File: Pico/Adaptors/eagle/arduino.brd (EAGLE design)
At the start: 57.1 x 53.3 mm, 3 parts

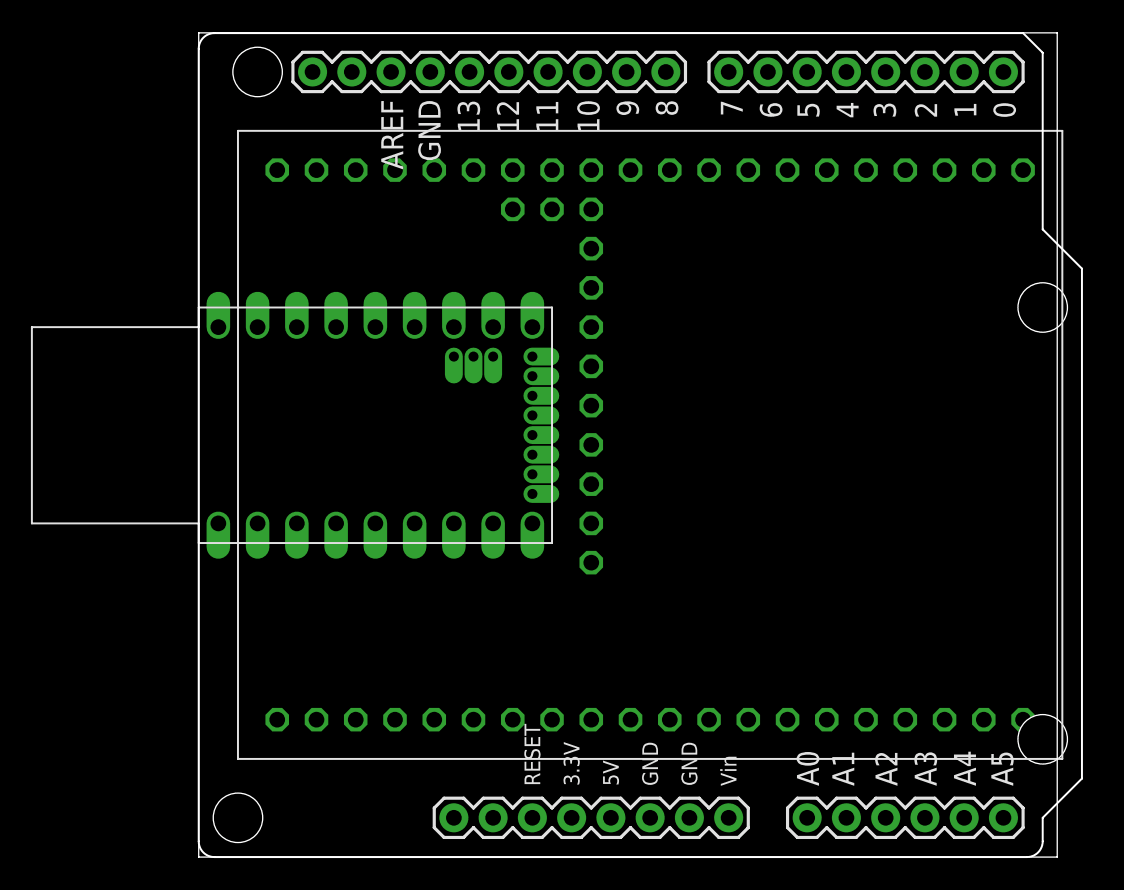
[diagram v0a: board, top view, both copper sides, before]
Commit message: nrf24 adaptor, and DRC
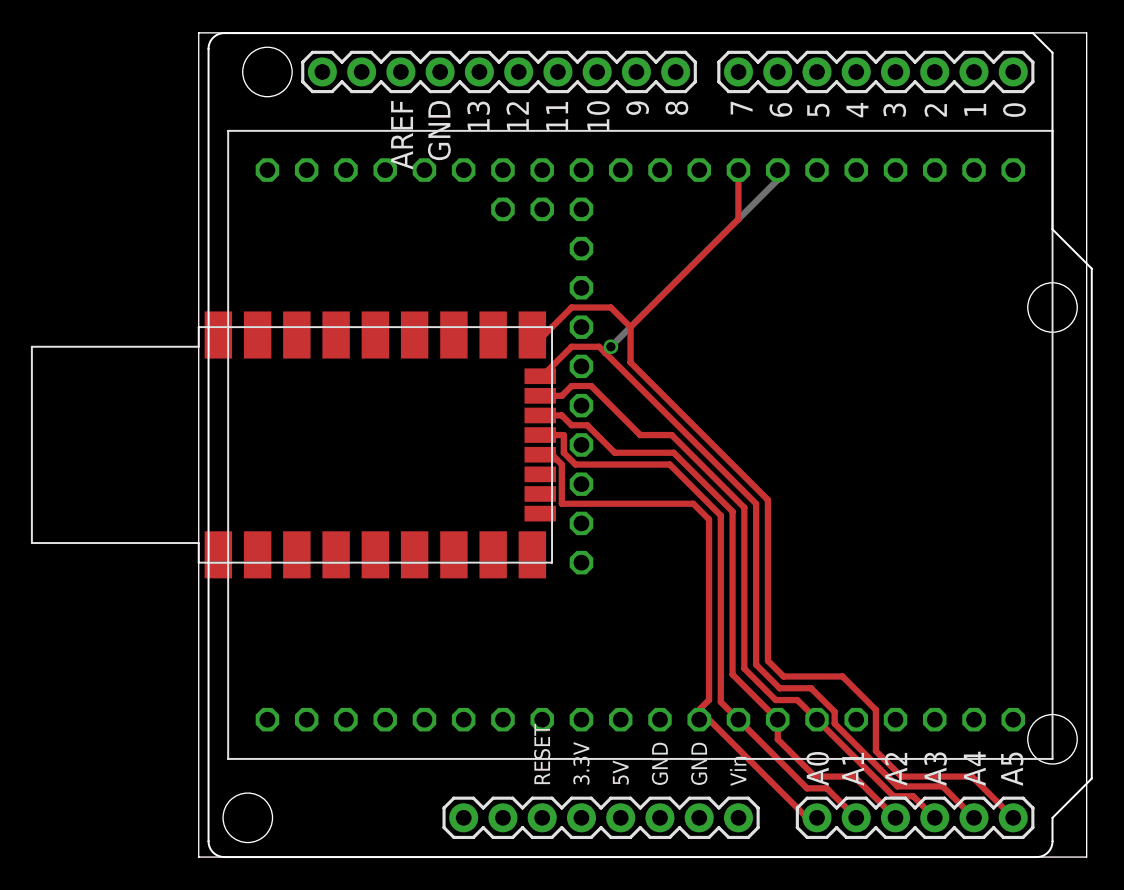
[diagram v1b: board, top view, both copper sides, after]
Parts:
- U$1: value ESPRUINO_PICO_PIN -> ESPRUINO_PICO_SMDONLY; device espruino_pico:ESPRUINO_PICO_PIN -> espruino_pico:ESPRUINO_PICO_SMDONLY
- moved U$1 1.27 mm to (15.2, 26.7)
- moved U$2 0.64 mm to (24.8, 26.7)
- moved U$3 0.64 mm to (28.6, 27.9)
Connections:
- new net A0: U$1.A0, U$2.A0, U$3.C0
- new net A1: U$1.A1, U$2.A1, U$3.C1
- new net A2: U$1.A2, U$2.A2, U$3.C2
- new net A3: U$1.A3, U$2.A3, U$3.C3
- new net A4: U$1.A4, U$2.A4, U$3.C4
- new net A5: U$1.A5, U$2.A5, U$3.C5
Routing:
- net A5: track 0.00 -> 67.6 mm
- net A4: track 0.00 -> 64.5 mm, vias 0 -> 1
- net A3: track 0.00 -> 43.5 mm
- net A2: track 0.00 -> 40.7 mm
- net A1: track 0.00 -> 38.4 mm
- net A0: track 0.00 -> 37.6 mm
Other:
- board size 57.1 x 53.3 mm -> 57.5 x 53.3 mm

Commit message: arduino adaptor
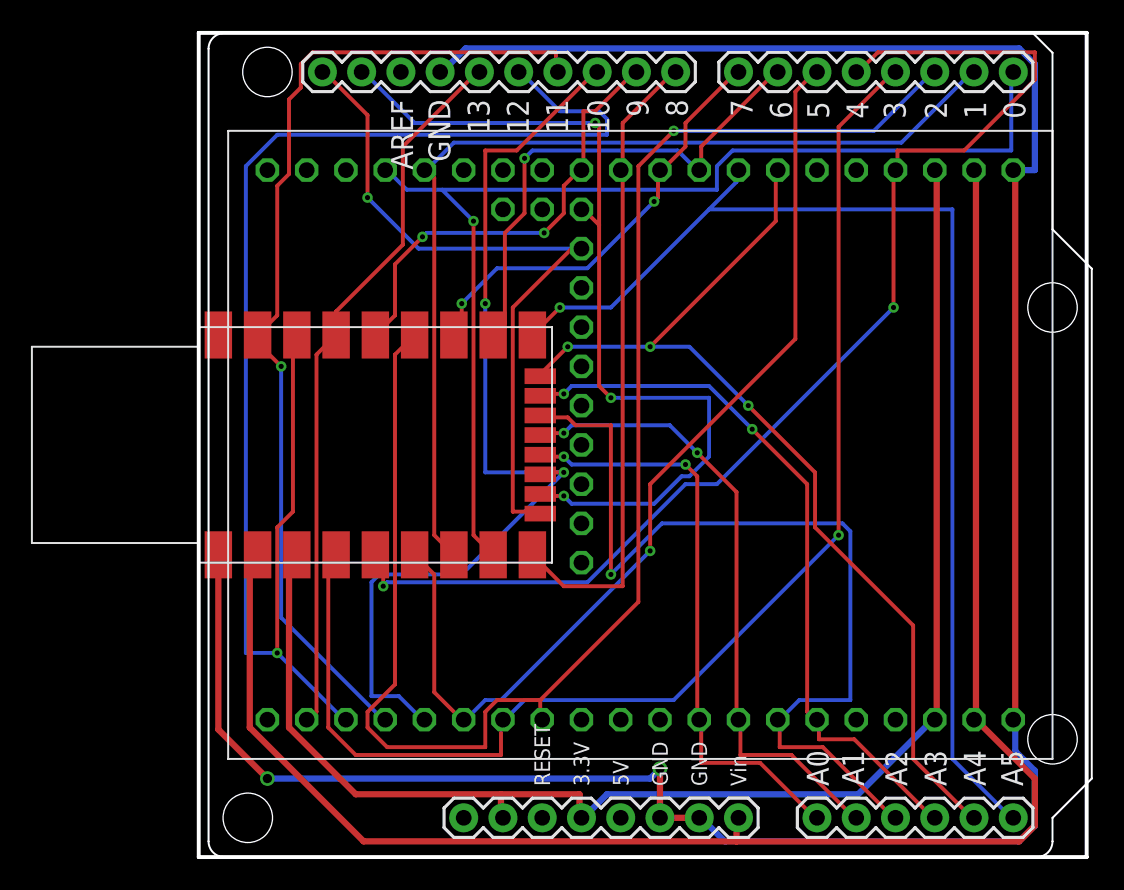
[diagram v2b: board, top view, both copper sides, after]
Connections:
- new net 3.3V: U$1.3.3V, U$2.3.3V, U$2.I/OREF, U$3.3.3, U$3.3.3.
- new net D0: U$1.B7, U$2.0, U$3.A10
- new net D1: U$1.B6, U$2.1, U$3.A9
- new net D10: U$1.A10, U$2.10, U$3.B6
- new net D11: U$1.B15, U$2.11, U$3.B5
- new net D12: U$1.B14, U$2.12, U$3.B4
- new net D13: U$1.B13, U$2.13, U$3.B3
- new net D2: U$1.B1, U$2.2, U$3.B9
- new net D3: U$1.B3, U$2.3, U$3.B8
- new net D4: U$1.B4, U$2.4, U$3.B13
- new net D5: U$1.B5, U$2.5, U$3.B7
- new net D6: U$1.A6, U$2.6, U$3.C6
- new net D7: U$1.A7, U$2.7, U$3.C7
- new net D8: U$1.A8, U$2.8, U$3.C8
- new net D9: U$1.B10, U$2.9, U$3.C9
- new net GND: U$1.GND, U$2.GND, U$2.GND., U$2.GND.., U$3.GND, U$3.GND.
- new net SCL: U$1.B8, U$2.SCL, U$3.B10
- new net SDA: U$1.B9, U$2.SDA, U$3.B11
- new net VIN: U$1.5V, U$2.VIN, U$3.VBAT, U$3.VBAT.
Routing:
- net GND: track 0.00 -> 161.1 mm, vias 0 -> 2
- net VIN: track 0.00 -> 111.6 mm
- net D2: track 0.00 -> 101.2 mm, vias 0 -> 1
- net 3.3V: track 0.00 -> 96.6 mm
- net D12: track 0.00 -> 93.1 mm, vias 0 -> 1
- net D3: track 0.00 -> 83.9 mm, vias 0 -> 1
- net D4: track 0.00 -> 77.8 mm, vias 0 -> 2
- net D0: track 0.00 -> 73.2 mm, vias 0 -> 1
- net D11: track 0.00 -> 65.3 mm, vias 0 -> 1
- net D5: track 0.00 -> 64.2 mm, vias 0 -> 1
- net D1: track 0.00 -> 63.9 mm
- net D10: track 0.00 -> 63.7 mm, vias 0 -> 2
- net SDA: track 0.00 -> 58.9 mm, vias 0 -> 3
- net D13: track 0.00 -> 46.7 mm
- net SCL: track 0.00 -> 45.8 mm, vias 0 -> 1
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
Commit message: tweaking
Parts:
- moved U$3 2.16 mm to (29.6, 29.8)
- moved U$1 0.76 mm to (16.0, 26.7)
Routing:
- net A2: track 59.1 -> 37.0 mm, vias 1 -> 2
- net D4: track 77.8 -> 56.2 mm, vias 2 -> 1
- net D12: track 93.1 -> 72.3 mm
- net D2: track 101.2 -> 84.9 mm
- net GND: track 161.1 -> 146.8 mm, vias 2 -> 0
- net A4: track 63.6 -> 77.5 mm, vias 3 -> 1
- net D1: track 63.9 -> 77.6 mm, vias 0 -> 1
- net SDA: track 58.9 -> 47.3 mm, vias 3 -> 0
- net A3: track 46.8 -> 56.4 mm, vias 2 -> 1
- net D5: track 64.2 -> 73.2 mm
- net SCL: track 45.8 -> 52.9 mm
- net A1: track 41.3 -> 34.8 mm
- net A5: track 75.0 -> 69.3 mm, vias 1 -> 2
- net D6: track 32.9 -> 27.2 mm
- net D0: track 73.2 -> 78.4 mm, vias 1 -> 0
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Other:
- board size 57.5 x 53.3 mm -> 57.1 x 53.3 mm

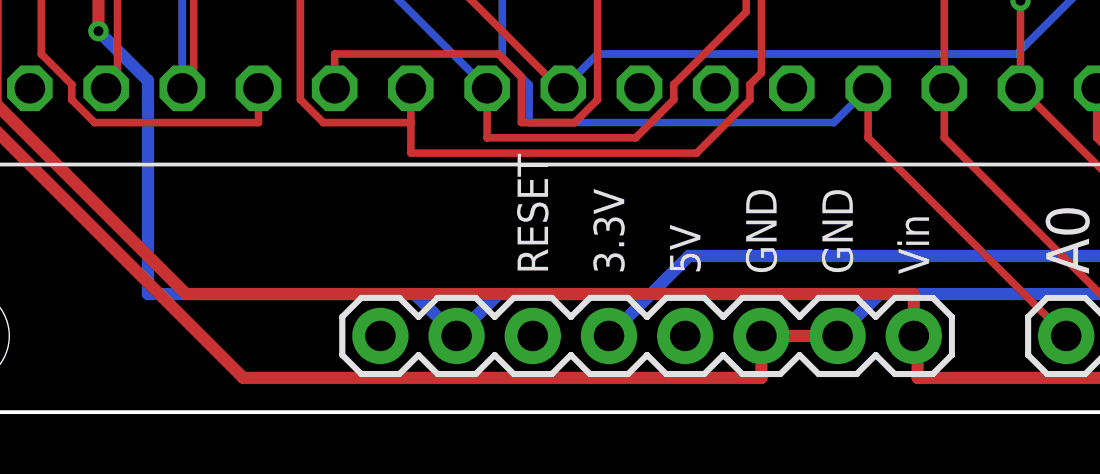
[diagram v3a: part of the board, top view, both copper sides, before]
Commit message: connect Vin and 5V, allowing shields to be powered from USB volts
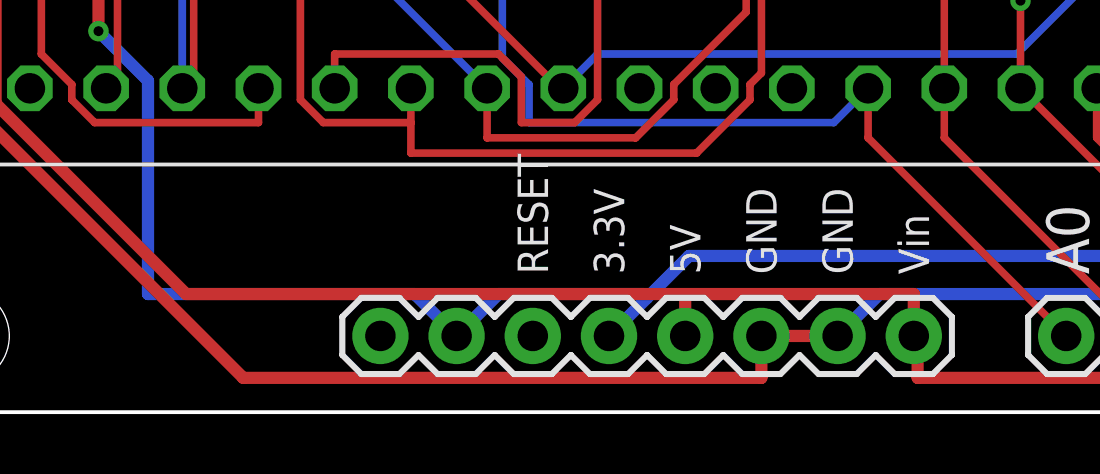
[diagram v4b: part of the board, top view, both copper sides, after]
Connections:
- net VIN: now also U$2.5V
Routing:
- net VIN: track 110.4 -> 111.8 mm
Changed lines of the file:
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@@
 <wire x1="4.318" y1="10.287" x2="4.318" y2="19.304" width="0.4064" layer="1"/>
 <wire x1="10.668" y1="3.937" x2="4.318" y2="10.287" width="0.4064" layer="1"/>
-<wire x1="34.925" y1="3.937" x2="10.668" y2="3.937" width="0.4064" layer="1"/>
+<wire x1="34.925" y1="3.937" x2="27.305" y2="3.937" width="0.4064" layer="1"/>
+<wire x1="27.305" y1="3.937" x2="10.668" y2="3.937" width="0.4064" layer="1"/>
 <wire x1="34.925" y1="2.54" x2="34.925" y2="3.937" width="0.4064" layer="1"/>
 <wire x1="52.959" y1="9.017" x2="51.181" y2="10.795" width="0.4064" layer="1"/>
@@
 <wire x1="35.052" y1="2.413" x2="35.052" y2="1.143" width="0.4064" layer="1"/>
 <wire x1="35.052" y1="2.413" x2="34.925" y2="2.54" width="0.4064" layer="1"/>
+<contactref element="U$2" pad="5V"/>
+<wire x1="27.305" y1="2.54" x2="27.305" y2="3.937" width="0.4064" layer="1"/>
 </signal>
 <signal name="3.3V" class="1">

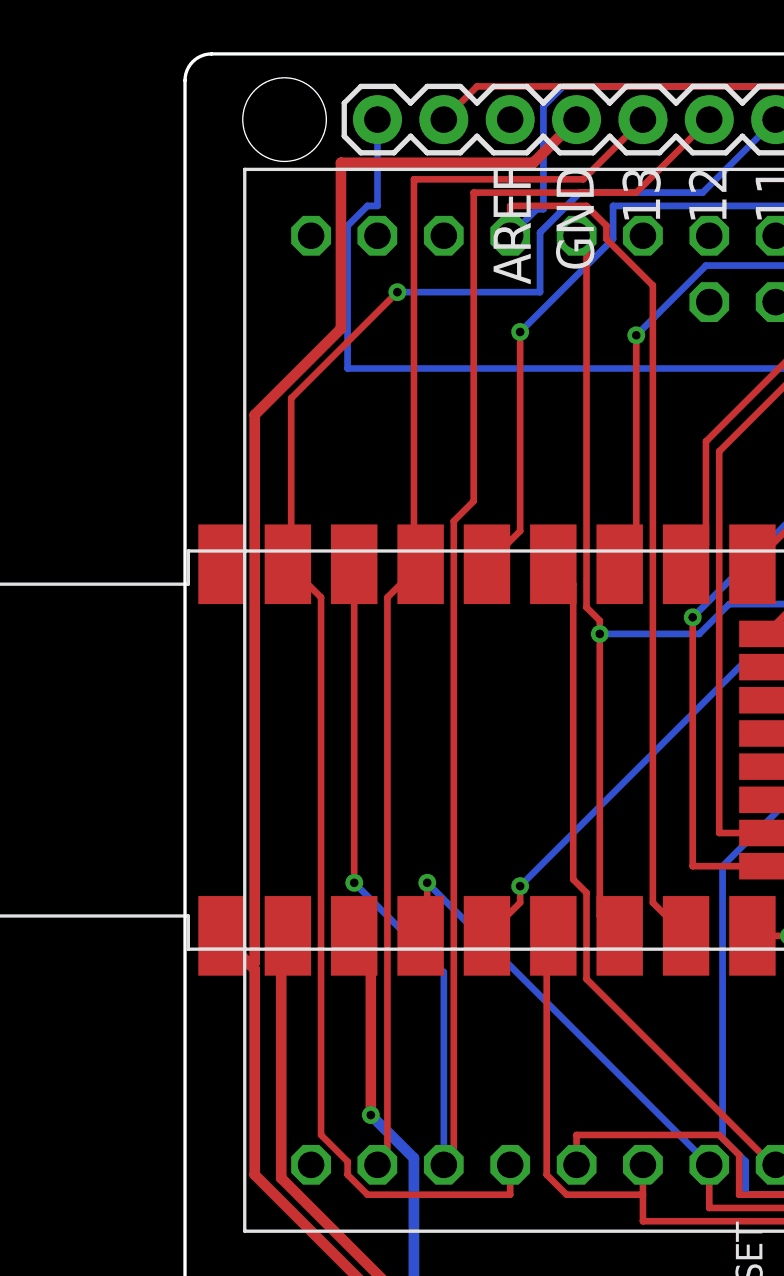
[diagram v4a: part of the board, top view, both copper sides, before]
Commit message: Add I2C pullup
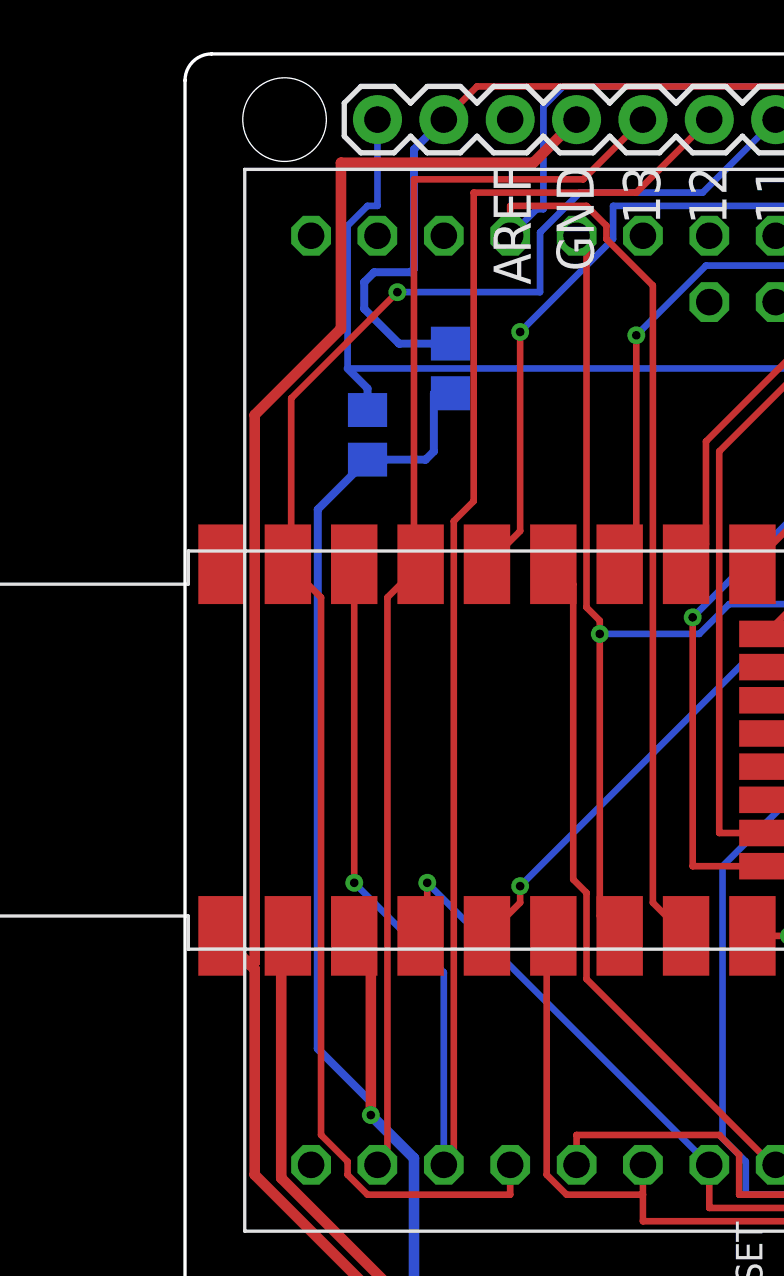
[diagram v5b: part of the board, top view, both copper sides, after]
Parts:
- added R1, R2: 10k, rcl:R0805
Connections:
- net 3.3V: now also R1.2, R2.2
- net SCL: now also R1.1
- net SDA: now also R2.1
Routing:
- net 3.3V: track 97.3 -> 129.5 mm
- net SDA: track 47.3 -> 60.5 mm
- net SCL: track 52.9 -> 54.8 mm
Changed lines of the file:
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@@
 <element name="U$3" library="espruino_pico" package="ESPRUINO" value="ESPRUINO" x="29.591" y="29.845"/>
 <element name="U$1" library="espruino_pico" package="ESPRUINO_PICO_SMDONLY" value="ESPRUINO_PICO_SMDONLY" x="16.002" y="26.67"/>
+<element name="R1" library="rcl" package="R0805" value="10k" x="7.62" y="38.735" rot="MR270"/>
+<element name="R2" library="rcl" package="R0805" value="10k" x="10.795" y="41.275" rot="MR270"/>
 </elements>
 <signals>
@@
 <wire x1="25.908" y1="3.937" x2="26.035" y2="3.81" width="0.4064" layer="16"/>
 <via x="7.747" y="12.7" extent="1-16" drill="0.3302"/>
+<contactref element="R1" pad="2"/>
+<contactref element="R2" pad="2"/>
+<wire x1="10.795" y1="40.325" x2="10.16" y2="40.325" width="0.3048" layer="16"/>
+<wire x1="10.16" y1="40.325" x2="10.16" y2="38.1" width="0.3048" layer="16"/>
+<wire x1="10.16" y1="38.1" x2="9.845" y2="37.785" width="0.3048" layer="16"/>
+<wire x1="9.845" y1="37.785" x2="7.62" y2="37.785" width="0.3048" layer="16"/>
+<wire x1="7.62" y1="37.785" x2="5.715" y2="35.88" width="0.3048" layer="16"/>
+<wire x1="5.715" y1="35.88" x2="5.715" y2="15.24" width="0.3048" layer="16"/>
+<wire x1="5.715" y1="15.24" x2="7.747" y2="13.208" width="0.3048" layer="16"/>
+<wire x1="7.747" y1="13.208" x2="7.747" y2="12.7" width="0.3048" layer="16"/>
 </signal>
 <signal name="SCL">
@@
 <wire x1="24.638" y1="41.275" x2="6.858" y2="41.275" width="0.254" layer="16"/>
 <via x="20.066" y="31.75" extent="1-16" drill="0.3302"/>
+<contactref element="R1" pad="1"/>
+<wire x1="6.858" y1="41.275" x2="7.62" y2="40.513" width="0.3048" layer="16"/>
+<wire x1="7.62" y1="40.513" x2="7.62" y2="39.685" width="0.3048" layer="16"/>
 </signal>
 <signal name="SDA">
@@
 <wire x1="24.511" y1="45.085" x2="24.511" y2="52.07" width="0.254" layer="1"/>
 <wire x1="25.781" y1="43.815" x2="24.511" y2="45.085" width="0.254" layer="1"/>
+<contactref element="R2" pad="1"/>
+<wire x1="10.541" y1="50.8" x2="9.398" y2="49.657" width="0.3048" layer="16"/>
+<wire x1="9.398" y1="49.657" x2="9.398" y2="45.085" width="0.3048" layer="16"/>
+<wire x1="9.398" y1="45.085" x2="9.271" y2="44.958" width="0.3048" layer="16"/>
+<wire x1="9.271" y1="44.958" x2="7.874" y2="44.958" width="0.3048" layer="16"/>
+<wire x1="7.874" y1="44.958" x2="7.493" y2="44.577" width="0.3048" layer="16"/>
+<wire x1="7.493" y1="44.577" x2="7.493" y2="43.561" width="0.3048" layer="16"/>
+<wire x1="7.493" y1="43.561" x2="8.829" y2="42.225" width="0.3048" layer="16"/>
+<wire x1="8.829" y1="42.225" x2="10.795" y2="42.225" width="0.3048" layer="16"/>
 </signal>
 <signal name="D13">

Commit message: move board around
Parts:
- moved U$2 0.64 mm to (24.1, 26.7)
- moved U$3 0.64 mm to (29.0, 29.8)
- moved R1 0.63 mm to (6.99, 38.7)
- moved R2 0.63 mm to (10.2, 41.3)
- moved U$1 0.63 mm to (15.4, 26.7)

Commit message: a full panel
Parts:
- added J1: JST-2P-SMD-PW-3410050P1, OPL Eagle Library:2P-SMD-2.0-90D
- U$1: value ESPRUINO_PICO_SMDONLY -> ESPRUINO_PICO_SMD; device espruino_pico:ESPRUINO_PICO_SMDONLY -> espruino_pico:ESPRUINO_PICO_SMD
- moved R1 4.84 mm to (8.89, 43.2), flipped to the top
- moved U$1 3.81 mm to (15.4, 22.9)
- moved R2 2.29 mm to (11.4, 43.2), flipped to the top
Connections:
- new net N$1: J1.+, U$1.BAT
- net GND: now also J1.-, J1.3, J1.4
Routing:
- net GND: track 146.8 -> 0.00 mm, vias 0 -> 40
- net D4: track 56.2 -> 106.7 mm, vias 1 -> 0
- net D0: track 78.4 -> 115.6 mm, vias 0 -> 1
- net SDA: track 60.5 -> 96.9 mm
- net D1: track 77.6 -> 109.7 mm, vias 1 -> 2
- net D12: track 72.3 -> 47.5 mm, vias 1 -> 0
- net D2: track 84.9 -> 107.5 mm, vias 1 -> 0
- net D5: track 73.2 -> 93.3 mm, vias 1 -> 0
- net A3: track 56.4 -> 36.6 mm, vias 1 -> 0
- net SCL: track 54.8 -> 70.6 mm, vias 1 -> 0
- net D10: track 65.2 -> 49.4 mm
- net VIN: track 111.8 -> 96.1 mm, vias 0 -> 1
- net A0: track 42.4 -> 27.6 mm, vias 1 -> 0
- net N$1: track 0.00 -> 12.8 mm
- net A4: track 77.5 -> 64.9 mm, vias 1 -> 0
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- added copper zone on layer 1, net GND
- added copper zone on layer 16, net GND
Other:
- board text added: "Espruino Arduino Adaptor rev 1.0"
- board text added: "espruino.com/ArduinoPico"
